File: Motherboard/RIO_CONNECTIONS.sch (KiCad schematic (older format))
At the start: 9 parts, among them U1 LM358, U2 LM358

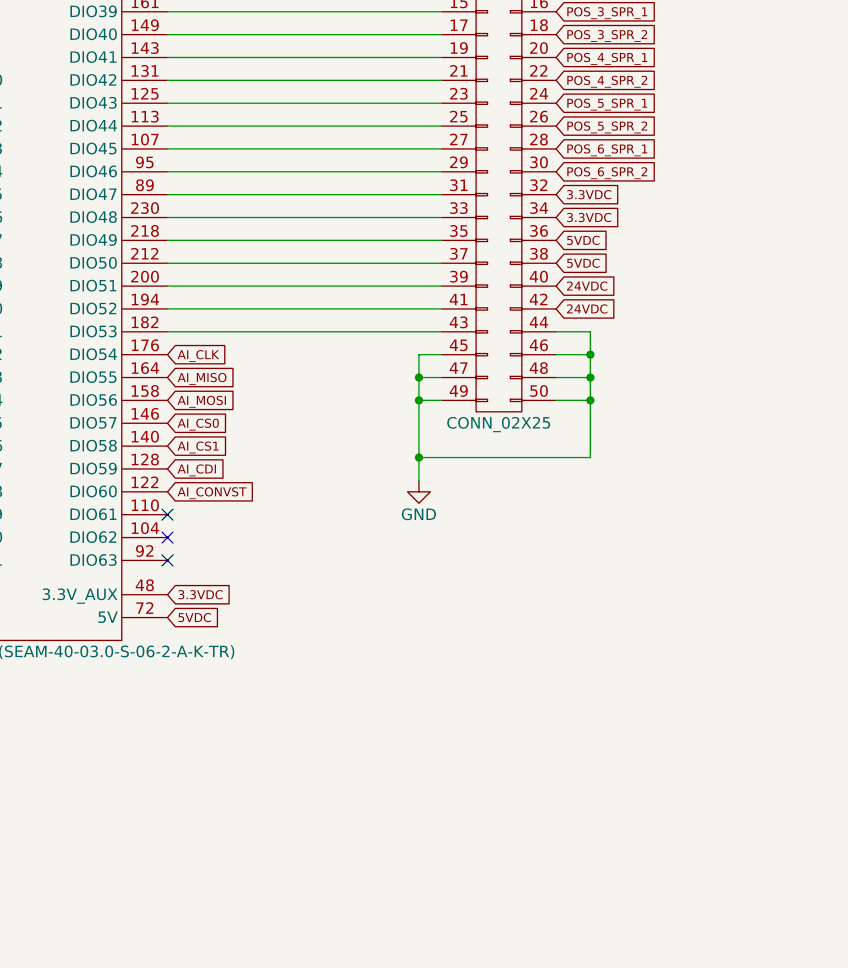
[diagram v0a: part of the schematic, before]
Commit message: - Refer to Google Drive BOM for list of changes for v1.1 - Create drawing for Hella BLDC controller plate.
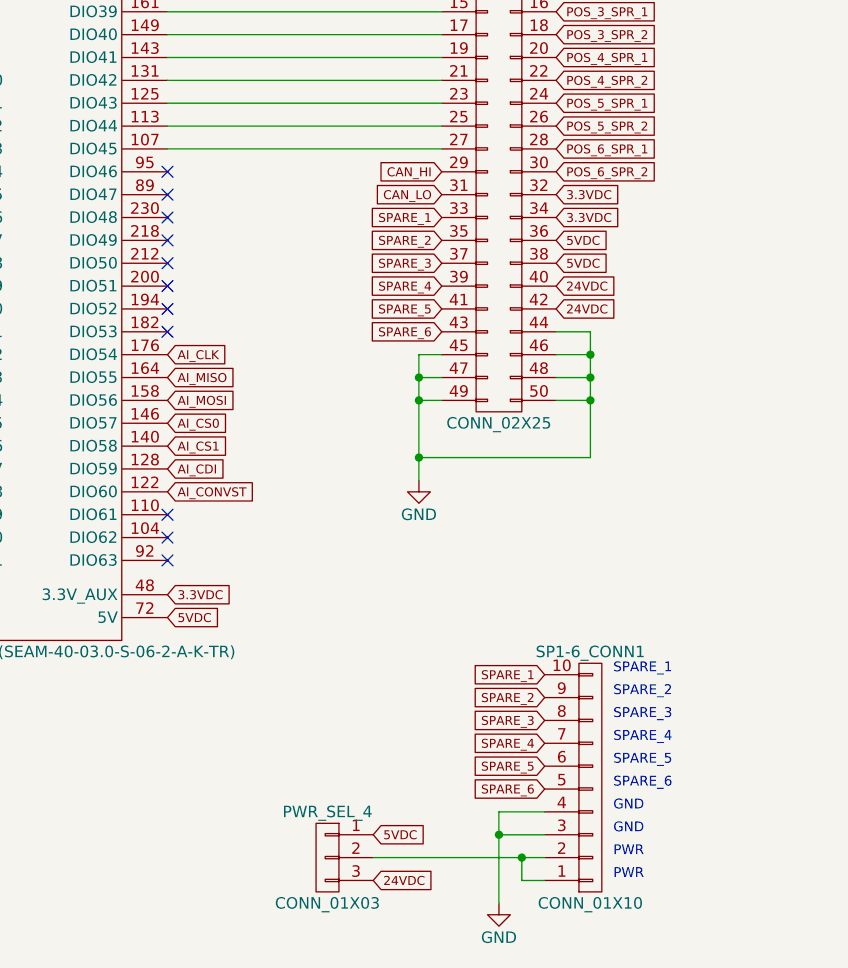
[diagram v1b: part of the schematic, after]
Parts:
- added PWR_SEL_4: CONN_01X03, Pin_Headers:Pin_Header_Straight_1x03_Pitch2.54mm, symbol CONN_01X03
- added SP1-6_CONN1: CONN_01X10, Smart_Tank:PHX_TB_HDR_10_POS_STR_(1755817), symbol CONN_01X10
- AO_CONN1: footprint Smart_Tank:PHX_TB_HDR_6_POS_(1757284) -> Smart_Tank:PHX_TB_HDR_6_POS_STR_(1755778)
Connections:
- net 24VDC: now also PWR_SEL_4.3 (P3)
- net 5VDC: now also PWR_SEL_4.1 (P1)
- net CAN_HI: now also EXPANSION_CONN1.29 (P29)
- net CAN_LO: now also EXPANSION_CONN1.31 (P31)
- net GND: now also SP1-6_CONN1.3 (P3), SP1-6_CONN1.4 (P4)
- net at RMC_CONN1.182 (DIO53): no longer EXPANSION_CONN1.43 (P43)
- net at RMC_CONN1.194 (DIO52): no longer EXPANSION_CONN1.41 (P41)
- net at RMC_CONN1.200 (DIO51): no longer EXPANSION_CONN1.39 (P39)
- net at RMC_CONN1.212 (DIO50): no longer EXPANSION_CONN1.37 (P37)
- net at RMC_CONN1.218 (DIO49): no longer EXPANSION_CONN1.35 (P35)
- net at RMC_CONN1.230 (DIO48): no longer EXPANSION_CONN1.33 (P33)
- net at RMC_CONN1.89 (DIO47): no longer EXPANSION_CONN1.31 (P31)
- net at RMC_CONN1.95 (DIO46): no longer EXPANSION_CONN1.29 (P29)
- new net: PWR_SEL_4.2 (P2), SP1-6_CONN1.1 (P1), SP1-6_CONN1.2 (P2)
- new net SPARE_1: EXPANSION_CONN1.33 (P33), SP1-6_CONN1.10 (P10)
- new net SPARE_2: EXPANSION_CONN1.35 (P35), SP1-6_CONN1.9 (P9)
- new net SPARE_3: EXPANSION_CONN1.37 (P37), SP1-6_CONN1.8 (P8)
- new net SPARE_4: EXPANSION_CONN1.39 (P39), SP1-6_CONN1.7 (P7)
- new net SPARE_5: EXPANSION_CONN1.41 (P41), SP1-6_CONN1.6 (P6)
- new net SPARE_6: EXPANSION_CONN1.43 (P43), SP1-6_CONN1.5 (P5)
- no-connect marks 24 -> 32
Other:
- note added: "PWR"
- note added: "SPARE_1"
- note added: "SPARE_2"
- note added: "SPARE_3"
- note added: "SPARE_4"
- note added: "SPARE_5"
- note added: "SPARE_6"
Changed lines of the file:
@@
 	2600 3300 3800 3300
-Wire Wire Line
-	3800 3400 2600 3400
-Wire Wire Line
-	2600 3500 3800 3500
-Wire Wire Line
-	2600 3600 3800 3600
-Wire Wire Line
-	3800 3700 2600 3700
-Wire Wire Line
-	2600 3800 3800 3800
-Wire Wire Line
-	3800 3900 2600 3900
-Wire Wire Line
-	2600 4000 3800 4000
-Wire Wire Line
-	2600 4100 3800 4100
 Wire Wire Line
 	3800 4200 3700 4200
@@
 F 0 "AO_CONN1" H 9650 3250 50  0000 C CNN
 F 1 "CONN_01X06" H 9650 2550 50  0000 C CNN
-F 2 "Smart_Tank:PHX_TB_HDR_6_POS_(1757284)" H 9650 2900 50  0001 C CNN
+F 2 "Smart_Tank:PHX_TB_HDR_6_POS_STR_(1755778)" H 9650 2900 50  0001 C CNN
 F 3 "" H 9650 2900 50  0000 C CNN
 	1    9650 2900
@@
 	4300 4100 4450 4100
 Connection ~ 4450 4200
+$Comp
+L CONN_01X10 SP1-6_CONN1
+U 1 1 5979F58B
+P 4450 6050
+F 0 "SP1-6_CONN1" H 4450 5500 50  0000 C CNN
+F 1 "CONN_01X10" H 4450 6600 50  0000 C CNN
+F 2 "Smart_Tank:PHX_TB_HDR_10_POS_STR_(1755817)" H 4450 6050 50  0001 C CNN
+F 3 "" H 4450 6050 50  0001 C CNN
+	1    4450 6050
+	1    0    0    1
+$EndComp
+Text Notes 4550 6500 0    43   ~ 0
+PWR
+Text Notes 4550 6400 0    43   ~ 0
+PWR
+Text Notes 4550 6300 0    43   ~ 0
+GND
+Text Notes 4550 6200 0    43   ~ 0
+GND
+Text Notes 4550 5600 0    43   ~ 0
+SPARE_1
+Text Notes 4550 5700 0    43   ~ 0
+SPARE_2
+Text Notes 4550 5800 0    43   ~ 0
+SPARE_3
+Text Notes 4550 5900 0    43   ~ 0
+SPARE_4
+Text Notes 4550 6000 0    43   ~ 0
+SPARE_5
+Text Notes 4550 6100 0    43   ~ 0
+SPARE_6
+Text GLabel 3800 3600 0    39   Input ~ 0
+SPARE_1
+Text GLabel 3800 3700 0    39   Input ~ 0
+SPARE_2
+Text GLabel 3800 3800 0    39   Input ~ 0
+SPARE_3
+Text GLabel 3800 3900 0    39   Input ~ 0
+SPARE_4
+Text GLabel 3800 4000 0    39   Input ~ 0
+SPARE_5
+Text GLabel 3800 4100 0    39   Input ~ 0
+SPARE_6
+Text GLabel 4250 5600 0    39   Input ~ 0
+SPARE_1
+Text GLabel 4250 5700 0    39   Input ~ 0
+SPARE_2
+Text GLabel 4250 5800 0    39   Input ~ 0
+SPARE_3
+Text GLabel 4250 5900 0    39   Input ~ 0
+SPARE_4
+Text GLabel 4250 6000 0    39   Input ~ 0
+SPARE_5
+Text GLabel 4250 6100 0    39   Input ~ 0
+SPARE_6
+$Comp
+L CONN_01X03 PWR_SEL_4
+U 1 1 597A1182
+P 3300 6400
+F 0 "PWR_SEL_4" H 3300 6600 50  0000 C CNN
+F 1 "CONN_01X03" H 3300 6200 50  0000 C CNN
+F 2 "Pin_Headers:Pin_Header_Straight_1x03_Pitch2.54mm" H 3300 6400 50  0001 C CNN
+F 3 "" H 3300 6400 50  0001 C CNN
+	1    3300 6400
+	-1   0    0    -1
+$EndComp
+Wire Wire Line
+	3500 6400 4250 6400
+Wire Wire Line
+	4250 6500 4150 6500
+Wire Wire Line
+	4150 6500 4150 6400
+Connection ~ 4150 6400
+$Comp
+L GND #PWR010
+U 1 1 597A13CB
+P 4050 6600
+F 0 "#PWR010" H 4050 6350 50  0001 C CNN
+F 1 "GND" H 4050 6450 50  0000 C CNN
+F 2 "" H 4050 6600 50  0000 C CNN
+F 3 "" H 4050 6600 50  0000 C CNN
+	1    4050 6600
+	1    0    0    -1
+$EndComp
+Wire Wire Line
+	4050 6600 4050 6200
+Wire Wire Line
+	4050 6200 4250 6200
+Wire Wire Line
+	4250 6300 4050 6300
+Connection ~ 4050 6300
+Text GLabel 3500 6300 2    39   Input ~ 0
+5VDC
+Text GLabel 3500 6500 2    39   Input ~ 0
+24VDC
+NoConn ~ 2600 3600
+NoConn ~ 2600 3700
+NoConn ~ 2600 3800
+NoConn ~ 2600 3900
+NoConn ~ 2600 4000
+NoConn ~ 2600 4100
+Text GLabel 3800 3400 0    39   Input ~ 0
+CAN_HI
+Text GLabel 3800 3500 0    39   Input ~ 0
+CAN_LO
+NoConn ~ 2600 3400
+NoConn ~ 2600 3500
 $EndSCHEMATC

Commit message: - Created Modbus Adapter.
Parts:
- AO_CONN1: symbol CONN_01X06 -> Smart-Tank-Motherboard-rescue:CONN_01X06
- CAN_CONN1: symbol CONN_02X05 -> Smart-Tank-Motherboard-rescue:CONN_02X05
- EXPANSION_CONN1, RIO_AIO_CONN1: symbol CONN_02X25 -> Smart-Tank-Motherboard-rescue:CONN_02X25
- PWR_SEL_4: symbol CONN_01X03 -> Smart-Tank-Motherboard-rescue:CONN_01X03
- R19: symbol R -> Smart-Tank-Motherboard-rescue:R
- RIO_PWR_CONN1: symbol CONN_01X02 -> Smart-Tank-Motherboard-rescue:CONN_01X02
- RMC_CONN1: symbol SAMTEC_CONN_(SEAM-40-03.0-S-06-2-A-K-TR) -> Smart-Tank-Motherboard-rescue:SAMTEC_CONN_(SEAM-40-03.0-S-06-2-A-K-TR)
- SP1-6_CONN1: symbol CONN_01X10 -> Smart-Tank-Motherboard-rescue:CONN_01X10
- U1, U2: symbol LM358 -> Smart-Tank-Motherboard-rescue:LM358
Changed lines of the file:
@@
-EESchema Schematic File Version 2
-LIBS:Smart Tank Motherboard-rescue
-LIBS:power
-LIBS:device
-LIBS:transistors
-LIBS:conn
-LIBS:linear
-LIBS:regul
-LIBS:74xx
-LIBS:cmos4000
-LIBS:adc-dac
-LIBS:memory
-LIBS:xilinx
-LIBS:microcontrollers
-LIBS:dsp
-LIBS:microchip
-LIBS:analog_switches
-LIBS:motorola
-LIBS:texas
-LIBS:intel
-LIBS:audio
-LIBS:interface
-LIBS:digital-audio
-LIBS:philips
-LIBS:display
-LIBS:cypress
-LIBS:siliconi
-LIBS:opto
-LIBS:atmel
-LIBS:contrib
-LIBS:valves
+EESchema Schematic File Version 4
 LIBS:Smart Tank Motherboard-cache
-EELAYER 25 0
+EELAYER 29 0
 EELAYER END
 $Descr A4 11693 8268
@@
 $EndDescr
 $Comp
-L SAMTEC_CONN_(SEAM-40-03.0-S-06-2-A-K-TR) RMC_CONN1
+L Smart-Tank-Motherboard-rescue:SAMTEC_CONN_(SEAM-40-03.0-S-06-2-A-K-TR) RMC_CONN1
 U 1 1 578FBA63
 P 1750 3950
@@
 24VDC
 $Comp
-L CONN_02X25 EXPANSION_CONN1
+L Smart-Tank-Motherboard-rescue:CONN_02X25 EXPANSION_CONN1
 U 1 1 578FCF49
 P 4050 3200
@@
 $EndComp
 $Comp
-L GND #PWR04
+L Smart-Tank-Motherboard-rescue:GND #PWR04
 U 1 1 578FD0EE
 P 3700 4750
@@
 POS_6_SPR_2
 $Comp
-L GND #PWR05
+L Smart-Tank-Motherboard-rescue:GND #PWR05
 U 1 1 578FD7C3
 P 1450 5250
@@
 AI_CONVST
 $Comp
-L CONN_02X05 CAN_CONN1
+L Smart-Tank-Motherboard-rescue:CONN_02X05 CAN_CONN1
 U 1 1 5790B1A2
 P 6550 1500
@@
 CAN_HI
 $Comp
-L CONN_02X25 RIO_AIO_CONN1
+L Smart-Tank-Motherboard-rescue:CONN_02X25 RIO_AIO_CONN1
 U 1 1 5790B5BC
 P 6550 4150
@@
 $EndComp
 $Comp
-L GND #PWR06
+L Smart-Tank-Motherboard-rescue:GND #PWR06
 U 1 1 5790B753
 P 6150 5650
@@
 AI15
 $Comp
-L CONN_01X02 RIO_PWR_CONN1
+L Smart-Tank-Motherboard-rescue:CONN_01X02 RIO_PWR_CONN1
 U 1 1 5790DCFC
 P 8300 1350
@@
 $EndComp
 $Comp
-L GND #PWR07
+L Smart-Tank-Motherboard-rescue:GND #PWR07
 U 1 1 5790E1D4
 P 7950 1500
@@
 5VDC
 $Comp
-L LM358 U1
+L Smart-Tank-Motherboard-rescue:LM358 U1
 U 1 1 57965B78
 P 8450 2650
@@
 $EndComp
 $Comp
-L LM358 U1
+L Smart-Tank-Motherboard-rescue:LM358 U1
 U 2 1 57965BB9
 P 8450 3600
@@
 $EndComp
 $Comp
-L LM358 U2
+L Smart-Tank-Motherboard-rescue:LM358 U2
 U 1 1 57965FA5
 P 8450 4550
@@
 $EndComp
 $Comp
-L GND #PWR08
+L Smart-Tank-Motherboard-rescue:GND #PWR08
 U 1 1 57966265
 P 8350 5950
@@
 	7800 5400 8150 5400
 $Comp
-L CONN_01X06 AO_CONN1
+L Smart-Tank-Motherboard-rescue:CONN_01X06 AO_CONN1
 U 1 1 57966E66
 P 9650 2900
@@
 NoConn ~ 1450 5100
 $Comp
-L R R19
+L Smart-Tank-Motherboard-rescue:R R19
 U 1 1 5798A433
 P 6550 2000
@@
 	5650 1400 6300 1400
 $Comp
-L LM358 U2
+L Smart-Tank-Motherboard-rescue:LM358 U2
 U 2 1 57A1F820
 P 8450 5500
@@
 $EndComp
 $Comp
-L GND #PWR09
+L Smart-Tank-Motherboard-rescue:GND #PWR09
 U 1 1 57A33686
 P 5650 1650
@@
 Connection ~ 4450 4200
 $Comp
-L CONN_01X10 SP1-6_CONN1
+L Smart-Tank-Motherboard-rescue:CONN_01X10 SP1-6_CONN1
 U 1 1 5979F58B
 P 4450 6050
@@
 SPARE_6
 $Comp
-L CONN_01X03 PWR_SEL_4
+L Smart-Tank-Motherboard-rescue:CONN_01X03 PWR_SEL_4
 U 1 1 597A1182
 P 3300 6400
@@
 Connection ~ 4150 6400
 $Comp
-L GND #PWR010
+L Smart-Tank-Motherboard-rescue:GND #PWR010
 U 1 1 597A13CB
 P 4050 6600

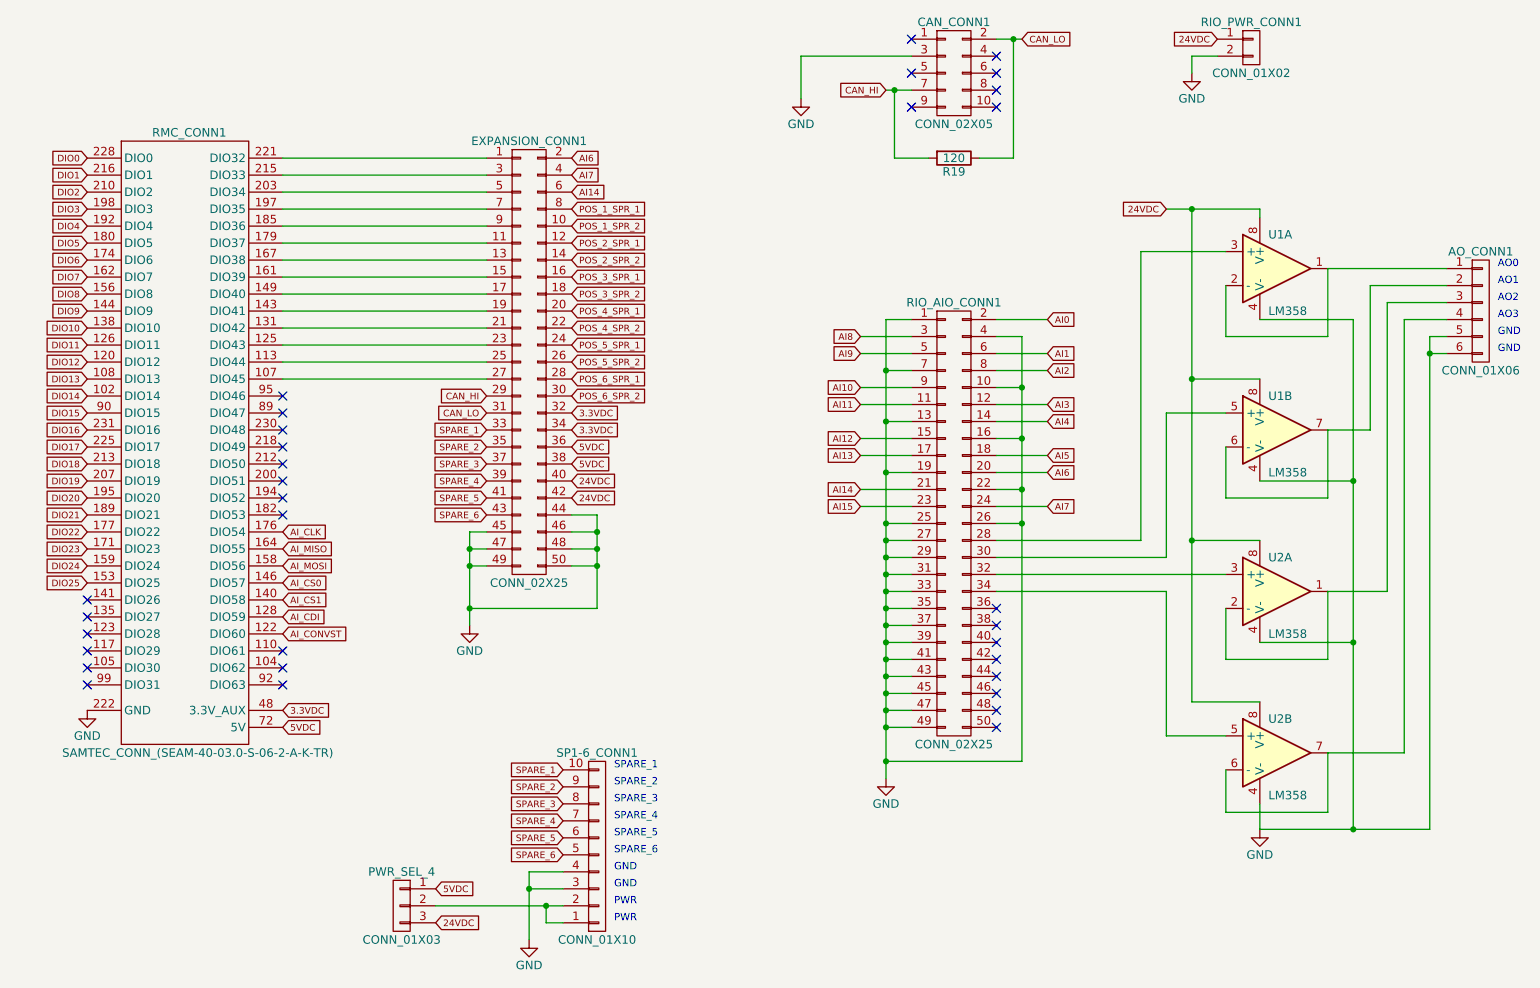
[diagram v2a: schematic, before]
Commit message: Committing what appears to be a bunch of backup files.  Haven't touched this project in a while, so I'm going for it.
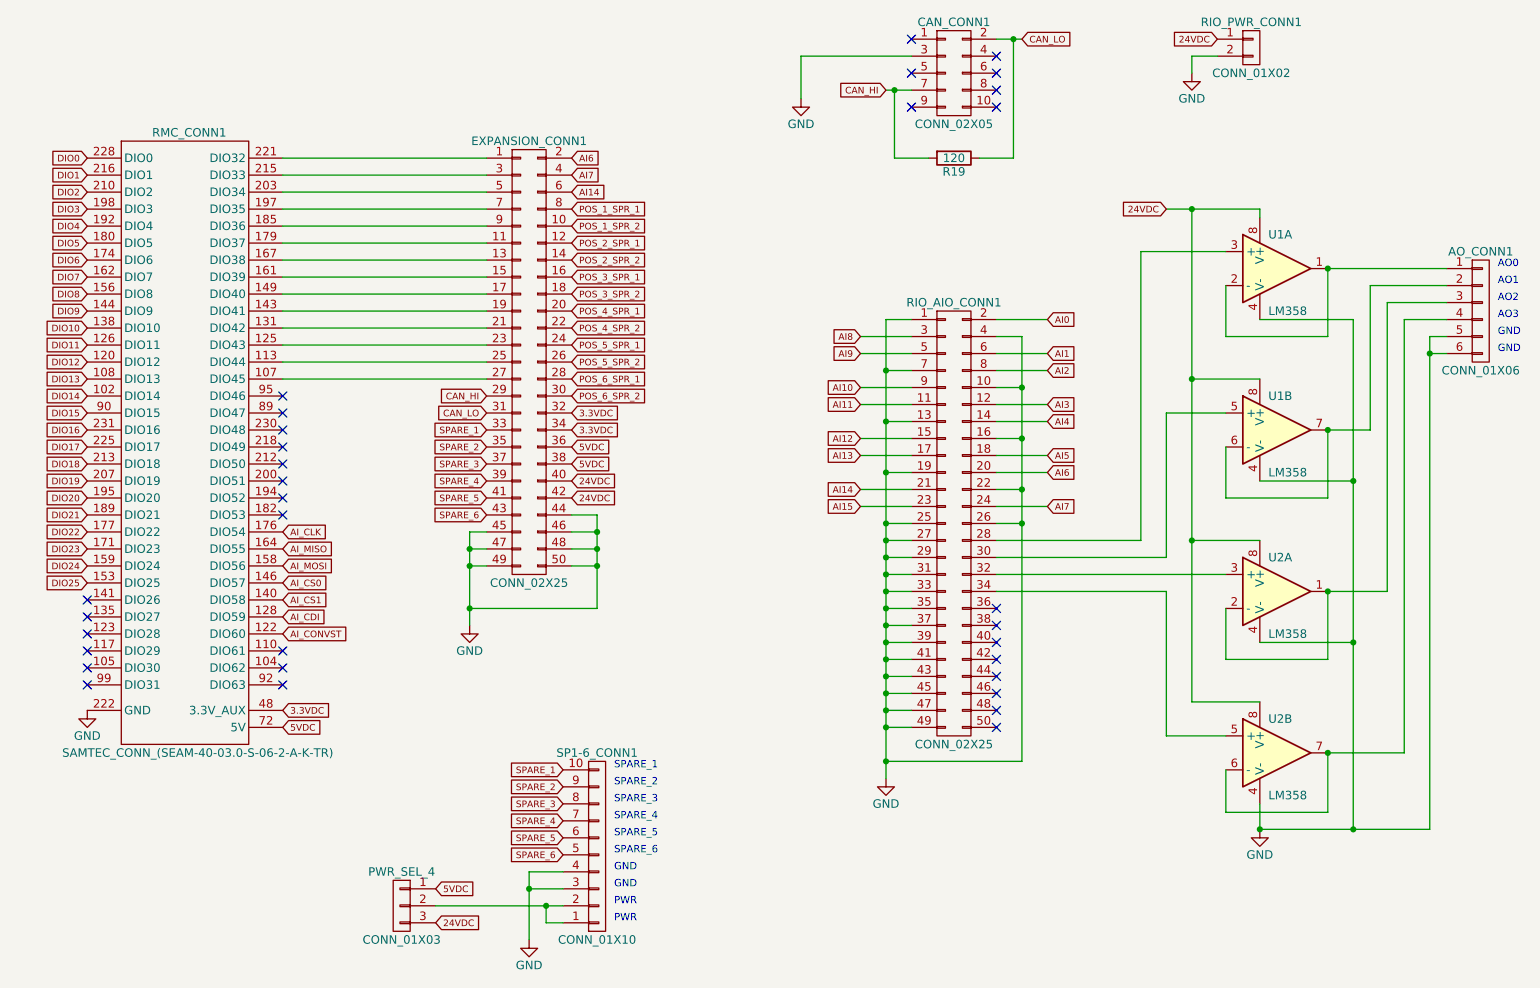
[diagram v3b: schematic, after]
